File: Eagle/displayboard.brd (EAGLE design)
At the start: 101.3 x 76.2 mm, 47 parts

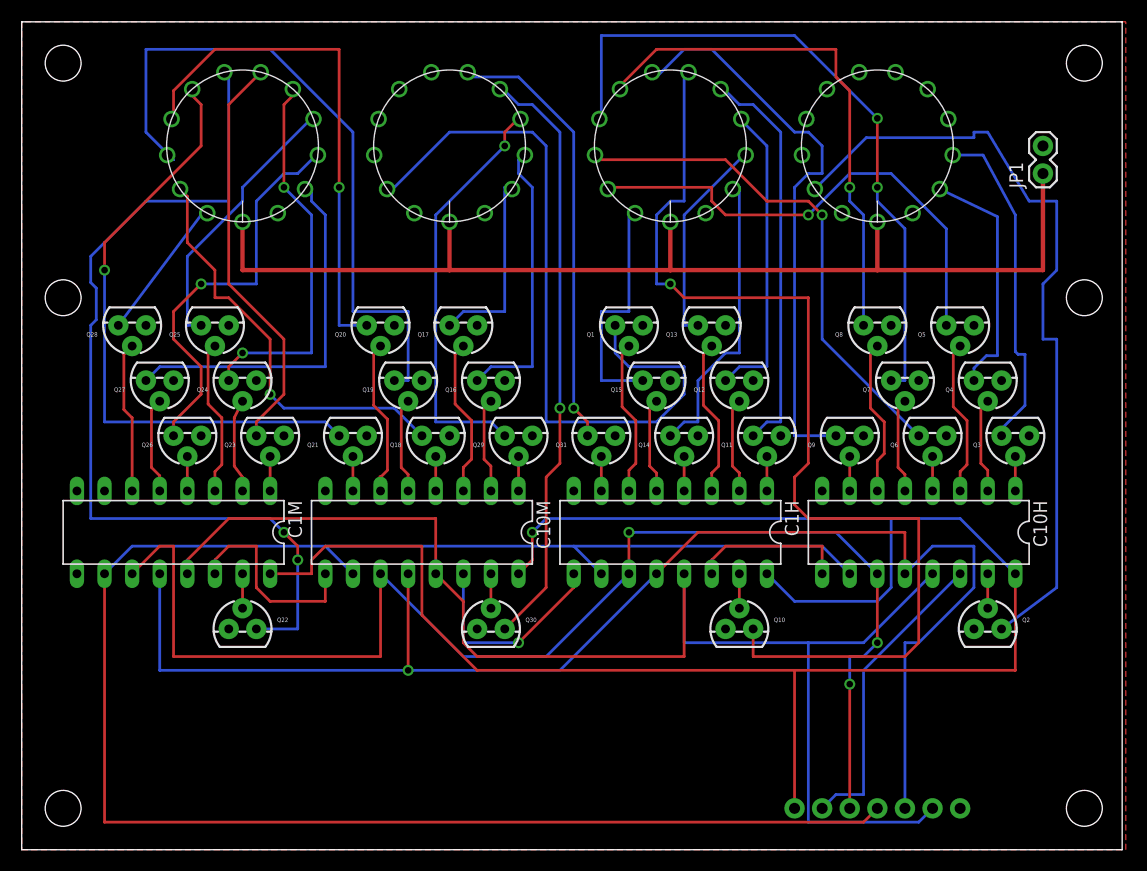
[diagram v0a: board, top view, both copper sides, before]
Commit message: Update schematic to include on-board 200V psu
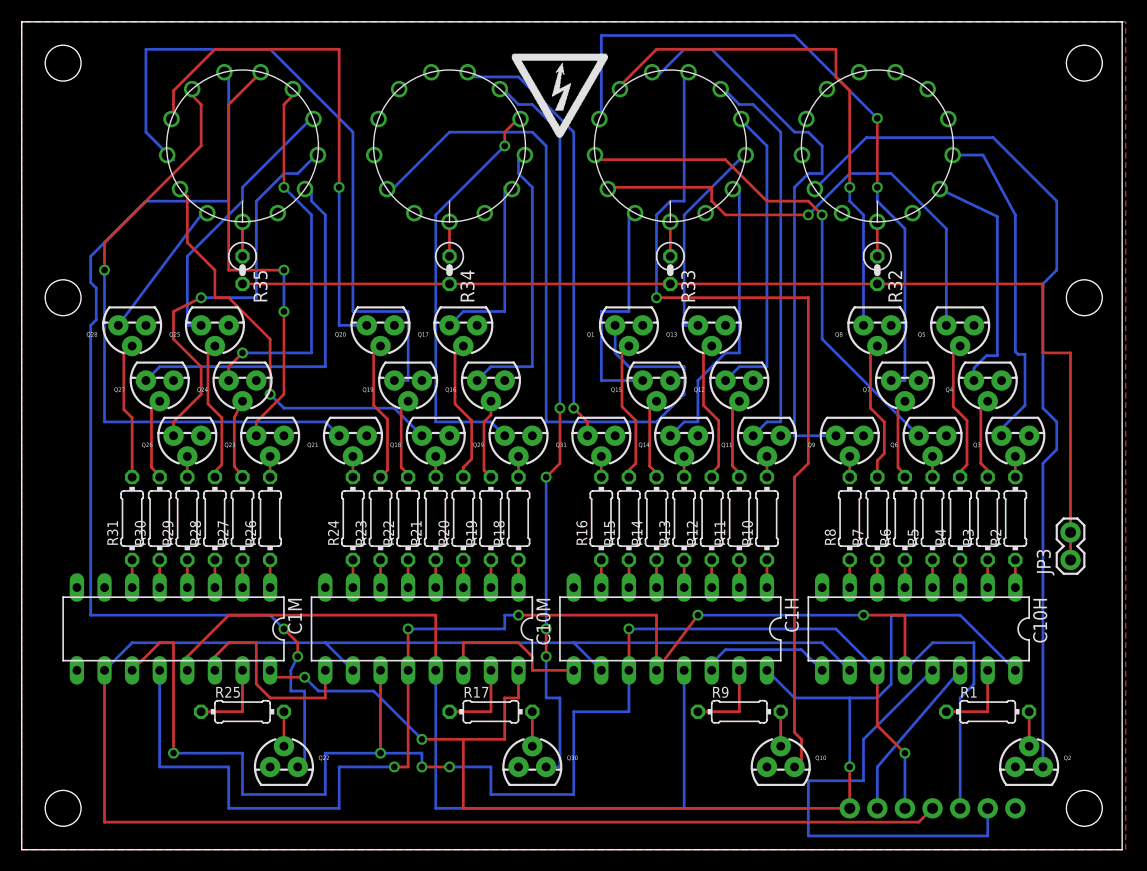
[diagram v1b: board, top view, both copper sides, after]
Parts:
- removed JP1: M02PTH, SparkFun-Connectors:1X02
- added JP3: M02PTH, SparkFun-Connectors:1X02
- added R1, R10, R11, R12, R13, R14, R15, R16, R17, R18, R19, R2, R20, R21, R22, R23, R24, R25, R26, R27, R28, R29, R3, R30, R31, R4, R5, R6, R7, R8, R9: 10k, resistor:0204/7
- added R32, R33, R34, R35: 15k, resistor:0207/2V
- added U$1: HIGHVOLTAGE, highvoltage:HIGHVOLTAGE
- moved Q30 13.3 mm to (47.0, 7.62)
- moved Q10 13.3 mm to (69.8, 7.62)
- moved Q2 13.3 mm to (92.7, 7.62)
- moved Q22 13.3 mm to (24.1, 7.62)
- moved C10H 8.89 mm to (82.5, 20.3)
- moved C10M 8.89 mm to (36.8, 20.3)
- moved C1H 8.89 mm to (59.7, 20.3)
- moved C1M 8.89 mm to (14.0, 20.3)
- moved JP2 5.08 mm to (91.4, 3.81)
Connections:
- new net N$100: N1H.ANODE, R33.1
- new net N$2: C10H.15, R1.1
- new net N$20: C10H.1, R2.1
- new net N$21: C10H.2, R3.1
- new net N$53: C10H.3, R4.1
- new net N$54: C10H.4, R5.1
- new net N$55: C10H.5, R6.1
- new net N$56: C10H.6, R7.1
- new net N$73: C10H.7, R8.1
- new net N$74: C1H.15, R9.1
- new net N$75: C1H.2, R11.1
- new net N$76: C1H.1, R10.1
- new net N$77: C1H.3, R12.1
- new net N$78: C1H.4, R13.1
- new net N$79: C1H.5, R14.1
- new net N$80: C1H.6, R15.1
- new net N$81: C1H.7, R16.1
- new net N$82: C10M.1, R18.1
- new net N$83: C10M.2, R19.1
- new net N$84: C10M.3, R20.1
- new net N$85: C10M.4, R21.1
- new net N$86: C10M.5, R22.1
- new net N$87: C10M.6, R23.1
- new net N$88: C10M.7, R24.1
- new net N$89: Q16.2, R19.2
- new net N$90: C1M.15, R25.1
- new net N$91: C1M.1, R26.1
- new net N$92: C1M.2, R27.1
- new net N$93: C1M.3, R28.1
- new net N$94: C1M.4, R29.1
- new net N$95: C1M.5, R30.1
- new net N$96: C1M.6, R31.1
- new net N$97: N10H.ANODE, R32.1
- new net N$98: N1M.ANODE, R35.1
- new net N$99: N10M.ANODE, R34.1
- net GND: no longer JP1.2
- net HV_VCC: now also JP3.1, JP3.2, R32.2, R33.2, R34.2, R35.2; no longer JP1.1, N10H.ANODE, N10M.ANODE, N1H.ANODE, N1M.ANODE
- net N$18: now also R1.2; no longer C10H.15
- net N$19: now also R2.2; no longer C10H.1
- net N$22: now also R3.2; no longer C10H.2
- net N$23: now also R4.2; no longer C10H.3
- net N$24: now also R5.2; no longer C10H.4
- net N$25: now also R6.2; no longer C10H.5
- net N$26: now also R7.2; no longer C10H.6
- net N$27: now also R8.2; no longer C10H.7
- net N$28: now also R9.2; no longer C1H.15
- net N$29: now also R10.2; no longer C1H.1
- net N$30: now also R11.2; no longer C1H.2
- net N$31: now also R12.2; no longer C1H.3
- net N$32: now also R13.2; no longer C1H.4
- net N$33: now also R14.2; no longer C1H.5
- net N$36: now also R15.2; no longer C1H.6
- net N$50: now also R17.2; no longer C10M.15
- net N$51: now also C10M.15, R17.1; no longer C10M.1, Q29.2
- net N$52: now also Q29.2, R18.2; no longer C10M.2, Q16.2
- net N$57: now also R25.2; no longer C1M.15
- net N$58: now also R26.2; no longer C1M.1
- net N$59: now also R27.2; no longer C1M.2
- net N$60: now also R28.2; no longer C1M.3
- net N$61: now also R29.2; no longer C1M.4
- net N$62: now also R30.2; no longer C1M.5
- net N$63: now also R31.2; no longer C1M.6
- net N$67: now also R16.2; no longer C1H.7
- net N$68: now also R20.2; no longer C10M.3
- net N$69: now also R23.2; no longer C10M.6
- net N$70: now also R21.2; no longer C10M.4
- net N$71: now also R22.2; no longer C10M.5
- net N$72: now also R24.2; no longer C10M.7
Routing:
- net 5V: track 171.2 -> 117.2 mm, vias 1 -> 3
- net N$10: track 97.2 -> 80.9 mm
- net N$16: track 55.0 -> 68.6 mm, vias 1 -> 4
- net N_SER: track 28.3 -> 15.5 mm
- net N$42: track 82.9 -> 93.5 mm
- net N$4: track 72.0 -> 80.3 mm
- net N$74: track 0.00 -> 7.62 mm
- net N$2: track 0.00 -> 7.62 mm
- net N$90: track 0.00 -> 7.62 mm
- net N$89: track 0.00 -> 7.51 mm
- net N_SCK: track 122.5 -> 129.4 mm, vias 3 -> 6
- net N$52: track 8.78 -> 1.91 mm
- net N_G: track 127.0 -> 132.5 mm
- net N$65: track 19.9 -> 14.5 mm, vias 1 -> 0
- net N_RCK: track 130.3 -> 134.9 mm, vias 1 -> 5
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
